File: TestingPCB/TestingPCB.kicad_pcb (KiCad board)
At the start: 2 copper layers, 90 x 80 mm, 19 parts, among them J1 Conn_01x04, J2 USB_C_Receptacle_USB2.0_14P, J4 Conn_01x10, U1 SC0915, U3 USBLC6-2P6, U4 CP2102N-Axx-xQFN20

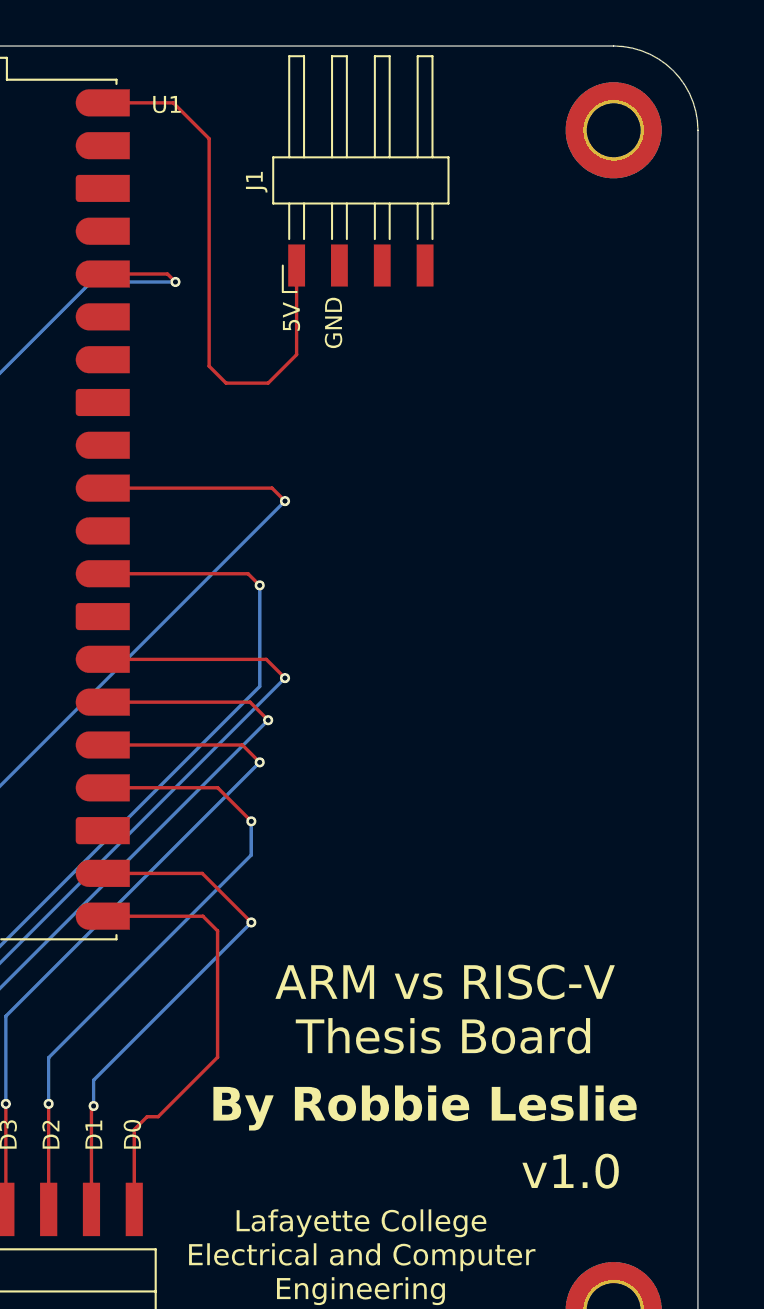
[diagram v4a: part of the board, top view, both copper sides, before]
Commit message: Fixed power pinout
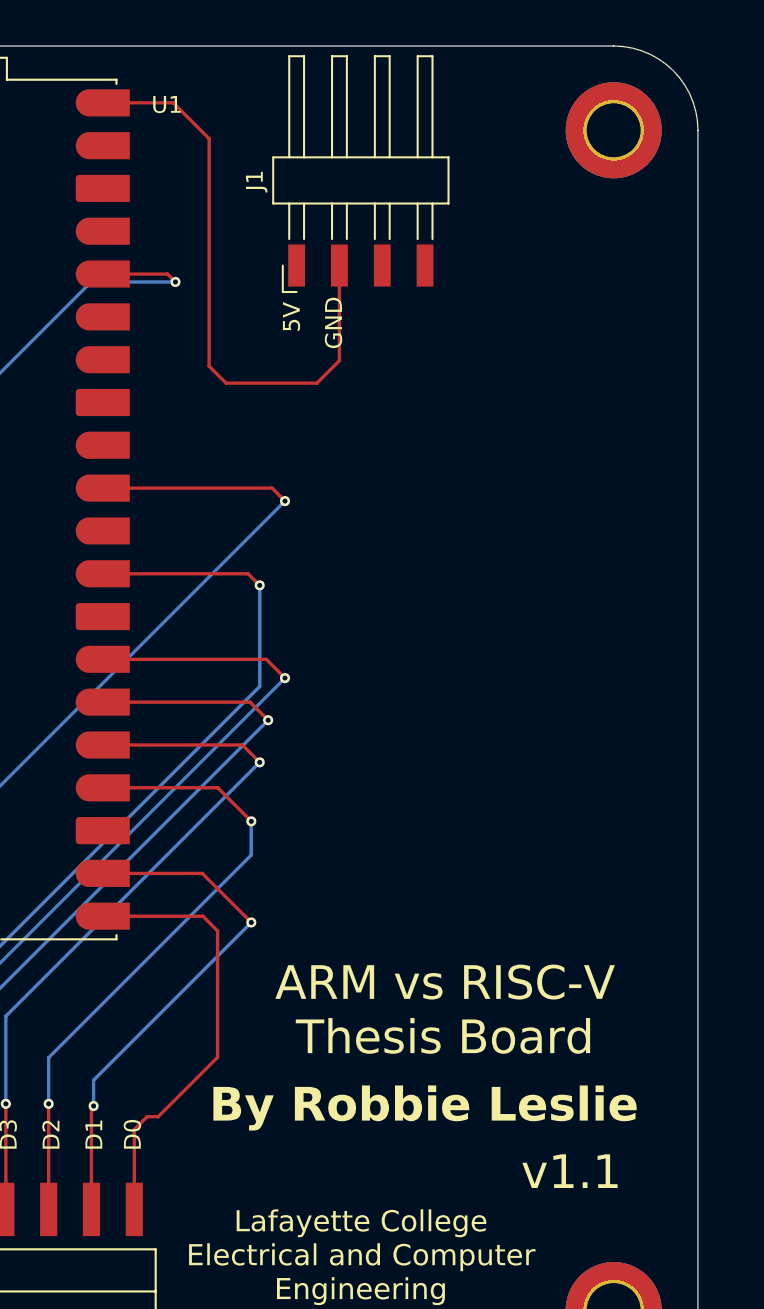
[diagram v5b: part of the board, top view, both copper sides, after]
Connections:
- J1 pad 1: /5V -> /GND
- J1 pad 2: /GND -> /5V
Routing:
- net /5V: track 32.3 -> 35.0 mm
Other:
- board text added: "v1.1"
- board text removed: "v1.0"
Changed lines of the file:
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@@
 	(title_block
 		(title "Thesis PCB")
-		(date "2025-03-10")
-		(rev "v1.0")
+		(date "2025-04-08")
+		(rev "v1.1")
 		(company "Lafayette College Electrical and Computer Engineering Department")
 		(comment 1 "By Robbie Leslie")
@@
 			)
 		)
+		(property "Manufacturer Part Number" "M20-8891045"
+			(at 0 0 0)
+			(unlocked yes)
+			(layer "F.Fab")
+			(hide yes)
+			(effects
+				(font
+					(size 1 1)
+					(thickness 0.15)
+				)
+			)
+		)
 		(property ki_fp_filters "Connector*:*_1x??_*")
 		(sheetname "Root")
@@
 			)
 		)
+		(property "Manufacturer Part Number" "CP2102N-A02-GQFN20R"
+			(at 0 0 0)
+			(unlocked yes)
+			(layer "F.Fab")
+			(hide yes)
+			(effects
+				(font
+					(size 1 1)
+					(thickness 0.15)
+				)
+			)
+		)
 		(property ki_fp_filters "SiliconLabs*QFN*3x3mm*P0.5mm*")
 		(sheetname "Root")
@@
 			(size 2.5 1)
 			(layers "F.Cu" "F.Paste" "F.Mask")
-			(net 5 "/5V")
+			(net 2 "/GND")
 			(pinfunction "Pin_1")
 			(pintype "passive")
@@
 			(size 2.5 1)
 			(layers "F.Cu" "F.Paste" "F.Mask")
-			(net 2 "/GND")
+			(net 5 "/5V")
 			(pinfunction "Pin_2")
 			(pintype "passive")
@@
 		)
 	)
-	(gr_text "v1.0"
+	(gr_text "v1.1"
 		(at 169.5 133 0)
 		(layer "F.SilkS")
@@
 	)
 	(segment
-		(start 148.87 68.37)
-		(end 144.69 68.37)
+		(start 151 70.5)
+		(end 151 84)
 		(width 0.2)
 		(layer "F.Cu")
@@
 	)
 	(segment
-		(start 156.19 78.025)
-		(end 156.19 83.31)
+		(start 158.73 83.67)
+		(end 158.73 78.025)
 		(width 0.2)
 		(layer "F.Cu")
@@
 	)
 	(segment
-		(start 154.5 85)
-		(end 152 85)
+		(start 152 85)
+		(end 157.4 85)
 		(width 0.2)
 		(layer "F.Cu")
@@
 	)
 	(segment
-		(start 152 85)
-		(end 151 84)
+		(start 151 84)
+		(end 152 85)
 		(width 0.2)
 		(layer "F.Cu")
@@
 	)
 	(segment
-		(start 151 70.5)
+		(start 144.69 68.37)
 		(end 148.87 68.37)
 		(width 0.2)
@@
 	)
 	(segment
-		(start 156.19 83.31)
-		(end 154.5 85)
+		(start 157.4 85)
+		(end 158.73 83.67)
 		(width 0.2)
 		(layer "F.Cu")
@@
 	)
 	(segment
-		(start 151 84)
+		(start 148.87 68.37)
 		(end 151 70.5)
 		(width 0.2)
